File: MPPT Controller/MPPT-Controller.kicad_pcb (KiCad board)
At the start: 4 copper layers, 99 x 99 mm, 99 parts, among them J1 Conn_01x02_Pin, J10 Conn_01x02_Pin, J11 Conn_01x02_Pin, J2 Conn_01x02_Pin, J3 Conn_01x02_Pin, J4 Conn_01x02_Pin, J5 USB_C_Receptacle_USB2.0_16P, J6 Conn_01x02_Pin, J7 Conn_01x02_Pin, J8 Conn_01x02_Pin, J9 Conn_01x02_Pin, M1 Fan_4pin, Q1 IRL540N, SW1 SW_SPDT, U1 ADS1115IDGS, U2 ESP32-WROOM-32D, U3 CH340C, U4 LM1117DT-3.3, U5 LM2596S-ADJ, U6 TC4422, U7 ADS1115IDGS

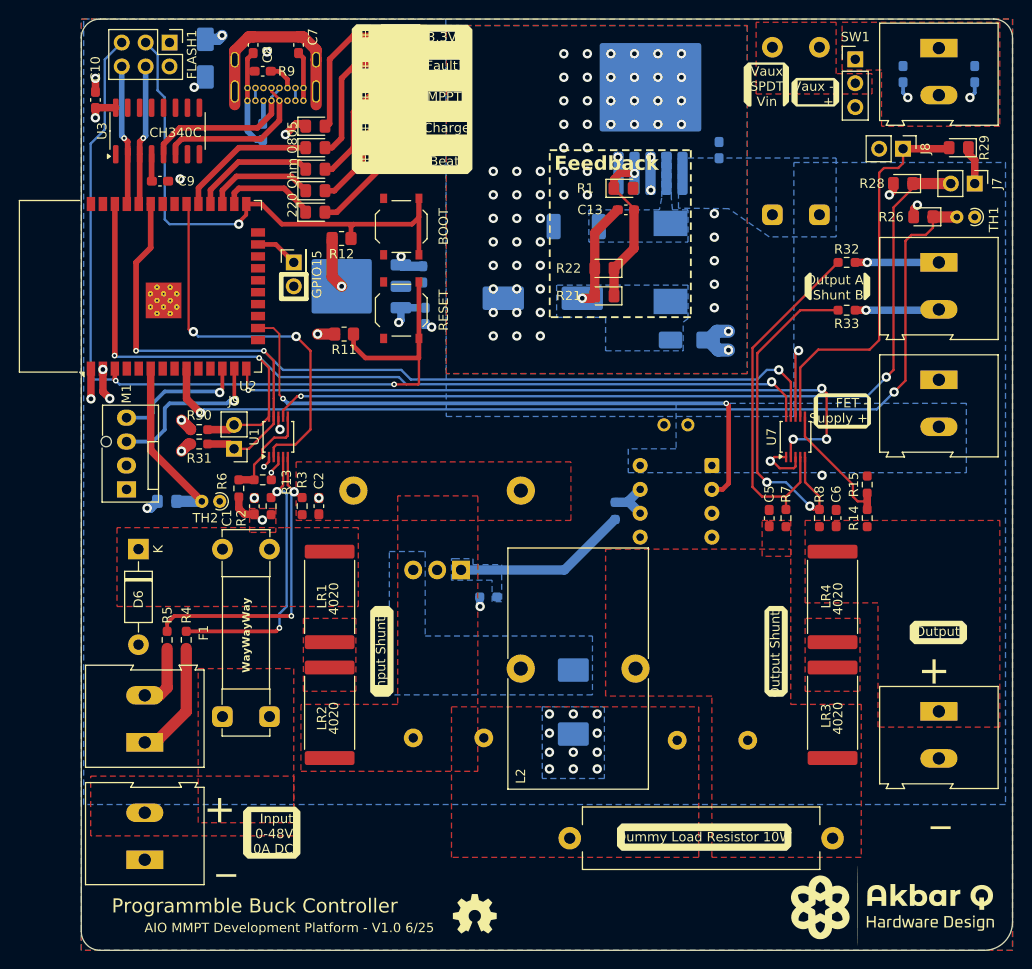
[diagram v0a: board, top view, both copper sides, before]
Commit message: Add Aux Hole for Heatsink
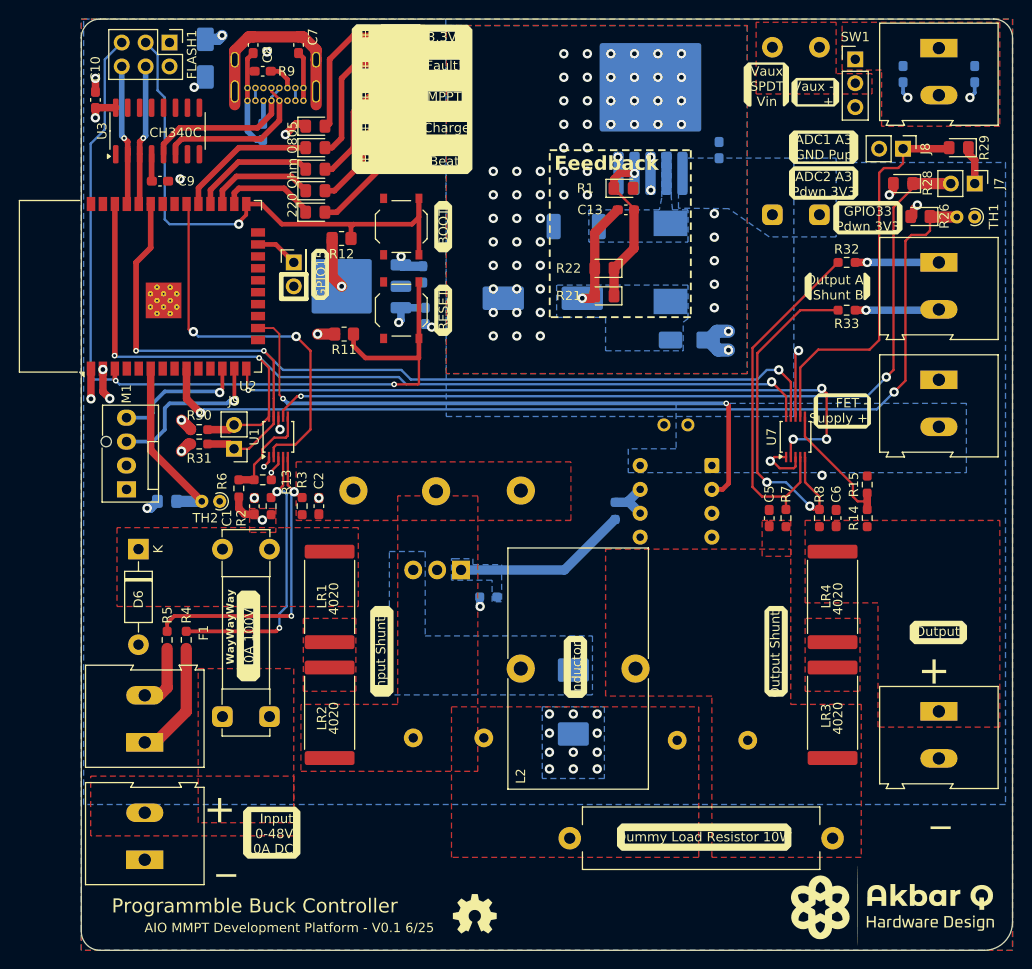
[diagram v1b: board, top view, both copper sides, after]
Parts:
- added ?: , , F.Cu at (80.7, 76.2)
- added G***: LOGO, LOGO, F.Cu at (97.0, 121.4)
- added G***: LOGO, LOGO, B.Cu at (57.1, 88.9)
- moved R26 0.32 mm to (132.2, 47.0)
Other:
- board text added: "10A 100V"
- board text added: "18mm"
- board text added: "ADC1 A3 GND Pup"
- board text added: "ADC2 A3 Pdwn 3V3"
- board text added: "ADS1115 ADC1 A1 A2"
- board text added: "ADS1115 ADC2 A1 A2"
- board text added: "AIO MMPT Development Platform - V0.1 6/25"
- board text added: "GPIO33 Pdwn 3V3"
- board text added: "Inductor"
- board text added: "TC4422"
- board text added: "Volt In 200kR/1kR ADC1 A2"
- board text added: "Volt Out 200kR/1kR ADC2 A2"
- board text removed: "ADS1115 Measure"
- board text removed: "AIO MMPT Development Platform - V1.0 6/25"

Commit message: Mod
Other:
- board text added: "5V GND FAN"
- board text added: "FLASH"

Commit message: Draft Pre Silk
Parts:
- removed the G*** at (57.1, 88.9)
- added G***: LOGO, LOGO, B.Cu at (155.5, 69.7)
- added G***: LOGO, LOGO, B.Cu at (132.8, 82.5)
- added G***: LOGO, LOGO, B.Cu at (121.2, 60.7)
- added G***: LOGO, LOGO, B.Cu at (27.3, 26.2)
- added G***: LOGO, LOGO, F.Cu at (97.0, 33.3)
- added G***: LOGO, LOGO, B.Cu at (154.5, 133.2)
- added G***: LOGO, LOGO, B.Cu at (54.1, 48.6)
- added G***: LOGO, LOGO, B.Cu at (41.5, 89.6)
- added G***: LOGO, LOGO, B.Cu at (74.7, 32.5)
- moved G*** 2.79 mm to (134.1, 81.8)
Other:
- board text added: "Fueled By the Undead"
- board text added: "{dblquote}Blessed are the bold, for they shall be masters of the world - Cursed are the righteous, for they shall be chained to the altar like slaves!{dblquote}"
